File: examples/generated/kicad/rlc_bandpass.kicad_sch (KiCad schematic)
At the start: 5 parts

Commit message: Attempt to correct strange wiring.
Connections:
- net GND: no longer C1.2, L1.1, L1.2, R1.2, R2.1
- new net: C1.2, L1.1, L1.2, R1.2, R2.1
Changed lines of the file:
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@@
     (stroke (width 0) (type solid) (color 0 0 0 0))
   )
-  (wire (pts (xy 106.35 70.00) (xy 100.00 70.00))
+  (wire (pts (xy 106.35 70.00) (xy 108.50 70.00))
     (stroke (width 0) (type solid) (color 0 0 0 0))
   )
-  (wire (pts (xy 100.00 70.00) (xy 100.00 89.00))
+  (wire (pts (xy 108.50 70.00) (xy 108.50 108.00))
     (stroke (width 0) (type solid) (color 0 0 0 0))
   )
-  (wire (pts (xy 93.65 108.00) (xy 100.00 108.00))
-    (stroke (width 0) (type solid) (color 0 0 0 0))
-  )
-  (wire (pts (xy 100.00 108.00) (xy 100.00 89.00))
+  (wire (pts (xy 108.50 108.00) (xy 93.65 108.00))
     (stroke (width 0) (type solid) (color 0 0 0 0))
   )
@@
     (stroke (width 0) (type solid) (color 0 0 0 0))
   )
-  (wire (pts (xy 100.00 108.00) (xy 100.00 98.00))
+  (wire (pts (xy 100.00 108.00) (xy 100.00 127.00))
     (stroke (width 0) (type solid) (color 0 0 0 0))
   )
-  (wire (pts (xy 100.00 139.65) (xy 100.00 98.00))
+  (wire (pts (xy 100.00 139.65) (xy 100.00 127.00))
     (stroke (width 0) (type solid) (color 0 0 0 0))
   )
-  (wire (pts (xy 93.65 184.00) (xy 100.00 184.00))
+  (wire (pts (xy 93.65 184.00) (xy 91.50 184.00))
     (stroke (width 0) (type solid) (color 0 0 0 0))
   )
-  (wire (pts (xy 100.00 184.00) (xy 100.00 98.00))
+  (wire (pts (xy 91.50 184.00) (xy 91.50 127.00))
     (stroke (width 0) (type solid) (color 0 0 0 0))
   )
-  (wire (pts (xy 50.00 62.38) (xy 71.83 62.38))
+  (wire (pts (xy 91.50 127.00) (xy 100.00 127.00))
     (stroke (width 0) (type solid) (color 0 0 0 0))
   )
-  (wire (pts (xy 71.83 62.38) (xy 71.83 66.19))
+  (wire (pts (xy 50.00 62.38) (xy 50.00 70.00))
     (stroke (width 0) (type solid) (color 0 0 0 0))
   )
-  (wire (pts (xy 93.65 70.00) (xy 71.83 70.00))
+  (wire (pts (xy 50.00 70.00) (xy 93.65 70.00))
     (stroke (width 0) (type solid) (color 0 0 0 0))
   )
-  (wire (pts (xy 71.83 70.00) (xy 71.83 66.19))
-    (stroke (width 0) (type solid) (color 0 0 0 0))
-  )
-  (junction (at 100.00 98.00) (diameter 1.016) (color 0 0 0 0))
+  (junction (at 100.00 127.00) (diameter 1.016) (color 0 0 0 0))
   (sheet_instances
     (path "/" (page "1"))

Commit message: Attempt shape and wiring fixes again.
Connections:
- net GND: now also R2.1; no longer R2.2
- new net: L1.1, R1.2
- new net: C1.2, L1.2, R2.2
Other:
- moved on the sheet: C1, L1, R1, R2, V1
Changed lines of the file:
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@@
     (comment 1 "Generated by mixedsig2cad")
   )
-  (symbol (lib_id "VSOURCE") (at 50.00 70.00 180) (unit 1)
+  (symbol (lib_id "VSOURCE") (at 56.00 86.00 180) (unit 1)
     (in_bom yes) (on_board yes)
-    (property "Reference" "V1" (at 50.0 60.0 0)
+    (property "Reference" "V1" (at 56.0 76.0 0)
       (effects (font (size 1.27 1.27)))
     )
-    (property "Value" "AC 1" (at 50.0 80.0 0)
+    (property "Value" "AC 1" (at 56.0 96.0 0)
       (effects (font (size 1.27 1.27)))
     )
@@
     )
   )
-  (symbol (lib_id "R") (at 100.00 70.00 90) (unit 1)
+  (symbol (lib_id "R") (at 90.00 78.00 90) (unit 1)
     (in_bom yes) (on_board yes)
-    (property "Reference" "R1" (at 100.0 62.0 0)
+    (property "Reference" "R1" (at 90.0 70.0 0)
       (effects (font (size 1.27 1.27)))
     )
-    (property "Value" "50" (at 100.0 78.0 0)
+    (property "Value" "50" (at 90.0 86.0 0)
       (effects (font (size 1.27 1.27)))
     )
@@
     )
   )
-  (symbol (lib_id "INDUCTOR") (at 100.00 108.00 0) (unit 1)
+  (symbol (lib_id "INDUCTOR") (at 120.00 78.00 0) (unit 1)
     (in_bom yes) (on_board yes)
-    (property "Reference" "L1" (at 100.0 100.0 0)
+    (property "Reference" "L1" (at 120.0 70.0 0)
       (effects (font (size 1.27 1.27)))
     )
-    (property "Value" "10m" (at 100.0 116.0 0)
+    (property "Value" "10m" (at 120.0 86.0 0)
       (effects (font (size 1.27 1.27)))
     )
@@
     )
   )
-  (symbol (lib_id "CAP") (at 100.00 146.00 180) (unit 1)
+  (symbol (lib_id "CAP") (at 120.00 112.00 180) (unit 1)
     (in_bom yes) (on_board yes)
-    (property "Reference" "C1" (at 100.0 138.0 0)
+    (property "Reference" "C1" (at 120.0 104.0 0)
       (effects (font (size 1.27 1.27)))
     )
-    (property "Value" "100n" (at 100.0 154.0 0)
+    (property "Value" "100n" (at 120.0 120.0 0)
       (effects (font (size 1.27 1.27)))
     )
@@
     )
   )
-  (symbol (lib_id "R") (at 100.00 184.00 90) (unit 1)
+  (symbol (lib_id "R") (at 142.00 130.00 180) (unit 1)
     (in_bom yes) (on_board yes)
-    (property "Reference" "R2" (at 100.0 176.0 0)
+    (property "Reference" "R2" (at 142.0 122.0 0)
       (effects (font (size 1.27 1.27)))
     )
-    (property "Value" "1k" (at 100.0 192.0 0)
+    (property "Value" "1k" (at 142.0 138.0 0)
       (effects (font (size 1.27 1.27)))
     )
@@
     )
   )
-  (symbol (lib_id "GND") (at 50.00 89.62 0) (unit 1)
+  (symbol (lib_id "GND") (at 56.00 105.62 0) (unit 1)
     (in_bom yes) (on_board yes)
-    (property "Reference" "#PWR0001" (at 50.0 85.81 0)
+    (property "Reference" "#PWR0001" (at 56.0 101.81 0)
       (effects (font (size 1.27 1.27)) hide)
     )
-    (property "Value" "GND" (at 50.0 93.43 0)
+    (property "Value" "GND" (at 56.0 109.43 0)
       (effects (font (size 1.27 1.27)))
     )
@@
     )
   )
-  (symbol (lib_id "GND") (at 100.00 164.35 0) (unit 1)
+  (symbol (lib_id "GND") (at 120.00 130.35 0) (unit 1)
     (in_bom yes) (on_board yes)
-    (property "Reference" "#PWR0002" (at 100.0 160.54 0)
+    (property "Reference" "#PWR0002" (at 120.0 126.53999999999999 0)
       (effects (font (size 1.27 1.27)) hide)
     )
-    (property "Value" "GND" (at 100.0 168.16 0)
+    (property "Value" "GND" (at 120.0 134.16 0)
       (effects (font (size 1.27 1.27)))
     )
@@
     )
   )
-  (symbol (lib_id "GND") (at 106.35 196.00 0) (unit 1)
+  (symbol (lib_id "GND") (at 142.00 148.35 0) (unit 1)
     (in_bom yes) (on_board yes)
-    (property "Reference" "#PWR0003" (at 106.35 192.19 0)
+    (property "Reference" "#PWR0003" (at 142.0 144.54 0)
       (effects (font (size 1.27 1.27)) hide)
     )
-    (property "Value" "GND" (at 106.35 199.81 0)
+    (property "Value" "GND" (at 142.0 152.16 0)
       (effects (font (size 1.27 1.27)))
     )
@@
     )
   )
-  (wire (pts (xy 50.00 77.62) (xy 50.00 89.62))
+  (wire (pts (xy 56.00 93.62) (xy 56.00 95.50))
     (stroke (width 0) (type solid) (color 0 0 0 0))
   )
-  (wire (pts (xy 100.00 152.35) (xy 100.00 164.35))
+  (wire (pts (xy 56.00 95.50) (xy 62.00 95.50))
     (stroke (width 0) (type solid) (color 0 0 0 0))
   )
-  (wire (pts (xy 106.35 184.00) (xy 106.35 196.00))
+  (wire (pts (xy 62.00 95.50) (xy 62.00 105.62))
     (stroke (width 0) (type solid) (color 0 0 0 0))
   )
-  (wire (pts (xy 106.35 70.00) (xy 108.50 70.00))
+  (wire (pts (xy 62.00 105.62) (xy 56.00 105.62))
     (stroke (width 0) (type solid) (color 0 0 0 0))
   )
-  (wire (pts (xy 108.50 70.00) (xy 108.50 108.00))
+  (wire (pts (xy 120.00 118.35) (xy 120.00 123.35))
     (stroke (width 0) (type solid) (color 0 0 0 0))
   )
-  (wire (pts (xy 108.50 108.00) (xy 93.65 108.00))
+  (wire (pts (xy 120.00 123.35) (xy 126.00 123.35))
     (stroke (width 0) (type solid) (color 0 0 0 0))
   )
-  (wire (pts (xy 106.35 108.00) (xy 100.00 108.00))
+  (wire (pts (xy 126.00 123.35) (xy 126.00 130.35))
     (stroke (width 0) (type solid) (color 0 0 0 0))
   )
-  (wire (pts (xy 100.00 108.00) (xy 100.00 127.00))
+  (wire (pts (xy 126.00 130.35) (xy 120.00 130.35))
     (stroke (width 0) (type solid) (color 0 0 0 0))
   )
-  (wire (pts (xy 100.00 139.65) (xy 100.00 127.00))
+  (wire (pts (xy 142.00 136.35) (xy 142.00 138.50))
     (stroke (width 0) (type solid) (color 0 0 0 0))
   )
-  (wire (pts (xy 93.65 184.00) (xy 91.50 184.00))
+  (wire (pts (xy 142.00 138.50) (xy 148.00 138.50))
     (stroke (width 0) (type solid) (color 0 0 0 0))
   )
-  (wire (pts (xy 91.50 184.00) (xy 91.50 127.00))
+  (wire (pts (xy 148.00 138.50) (xy 148.00 148.35))
     (stroke (width 0) (type solid) (color 0 0 0 0))
   )
-  (wire (pts (xy 91.50 127.00) (xy 100.00 127.00))
+  (wire (pts (xy 148.00 148.35) (xy 142.00 148.35))
     (stroke (width 0) (type solid) (color 0 0 0 0))
   )
-  (wire (pts (xy 50.00 62.38) (xy 50.00 70.00))
+  (wire (pts (xy 96.35 78.00) (xy 113.65 78.00))
     (stroke (width 0) (type solid) (color 0 0 0 0))
   )
-  (wire (pts (xy 50.00 70.00) (xy 93.65 70.00))
+  (wire (pts (xy 126.35 78.00) (xy 131.00 78.00))
     (stroke (width 0) (type solid) (color 0 0 0 0))
   )
-  (junction (at 100.00 127.00) (diameter 1.016) (color 0 0 0 0))
+  (wire (pts (xy 131.00 78.00) (xy 131.00 95.00))
+    (stroke (width 0) (type solid) (color 0 0 0 0))
+  )
+  (wire (pts (xy 120.00 105.65) (xy 120.00 95.00))
+    (stroke (width 0) (type solid) (color 0 0 0 0))
+  )
+  (wire (pts (xy 120.00 95.00) (xy 131.00 95.00))
+    (stroke (width 0) (type solid) (color 0 0 0 0))
+  )
+  (wire (pts (xy 142.00 123.65) (xy 142.00 95.00))
+    (stroke (width 0) (type solid) (color 0 0 0 0))
+  )
+  (wire (pts (xy 142.00 95.00) (xy 131.00 95.00))
+    (stroke (width 0) (type solid) (color 0 0 0 0))
+  )
+  (wire (pts (xy 56.00 78.38) (xy 56.00 78.00))
+    (stroke (width 0) (type solid) (color 0 0 0 0))
+  )
+  (wire (pts (xy 56.00 78.00) (xy 83.65 78.00))
+    (stroke (width 0) (type solid) (color 0 0 0 0))
+  )
+  (junction (at 131.00 95.00) (diameter 1.016) (color 0 0 0 0))
   (sheet_instances
     (path "/" (page "1"))

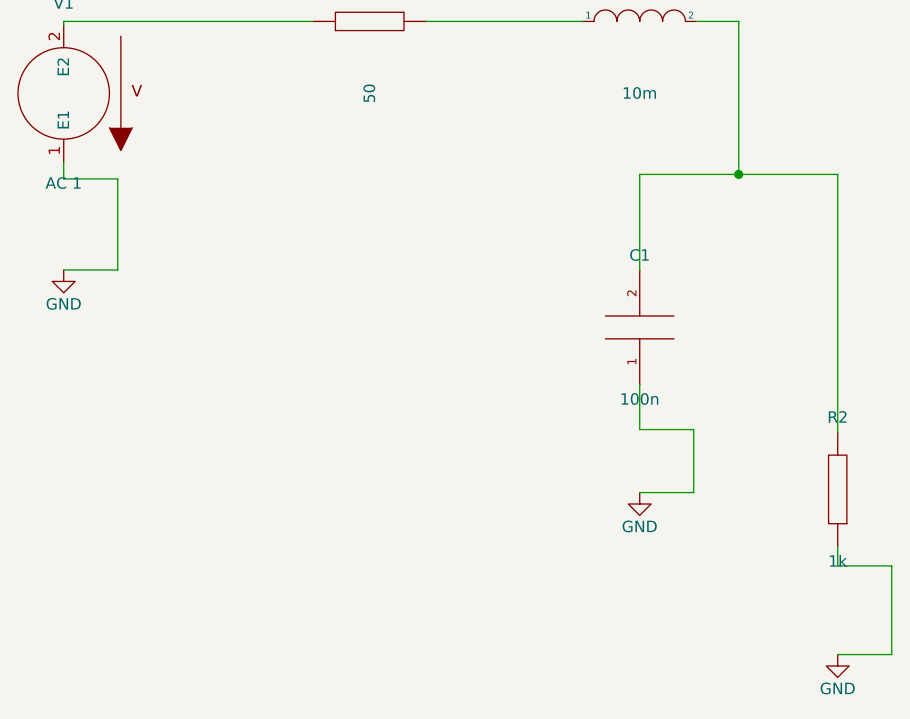
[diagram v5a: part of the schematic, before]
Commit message: Attempt to fix kinking and terminal direction issuses.
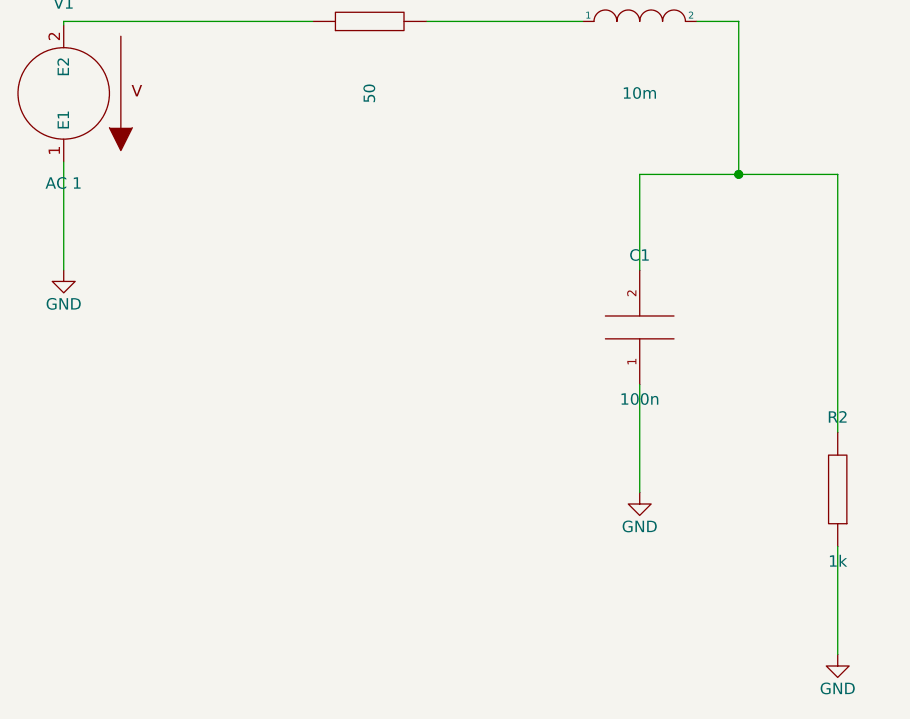
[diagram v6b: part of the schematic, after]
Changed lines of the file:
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@@
     )
   )
-  (wire (pts (xy 56.00 93.62) (xy 56.00 95.50))
+  (wire (pts (xy 56.00 93.62) (xy 56.00 105.62))
     (stroke (width 0) (type solid) (color 0 0 0 0))
   )
-  (wire (pts (xy 56.00 95.50) (xy 62.00 95.50))
+  (wire (pts (xy 120.00 118.35) (xy 120.00 130.35))
     (stroke (width 0) (type solid) (color 0 0 0 0))
   )
-  (wire (pts (xy 62.00 95.50) (xy 62.00 105.62))
+  (wire (pts (xy 142.00 136.35) (xy 142.00 148.35))
     (stroke (width 0) (type solid) (color 0 0 0 0))
   )
-  (wire (pts (xy 62.00 105.62) (xy 56.00 105.62))
-    (stroke (width 0) (type solid) (color 0 0 0 0))
-  )
-  (wire (pts (xy 120.00 118.35) (xy 120.00 123.35))
-    (stroke (width 0) (type solid) (color 0 0 0 0))
-  )
-  (wire (pts (xy 120.00 123.35) (xy 126.00 123.35))
-    (stroke (width 0) (type solid) (color 0 0 0 0))
-  )
-  (wire (pts (xy 126.00 123.35) (xy 126.00 130.35))
-    (stroke (width 0) (type solid) (color 0 0 0 0))
-  )
-  (wire (pts (xy 126.00 130.35) (xy 120.00 130.35))
-    (stroke (width 0) (type solid) (color 0 0 0 0))
-  )
-  (wire (pts (xy 142.00 136.35) (xy 142.00 138.50))
-    (stroke (width 0) (type solid) (color 0 0 0 0))
-  )
-  (wire (pts (xy 142.00 138.50) (xy 148.00 138.50))
-    (stroke (width 0) (type solid) (color 0 0 0 0))
-  )
-  (wire (pts (xy 148.00 138.50) (xy 148.00 148.35))
-    (stroke (width 0) (type solid) (color 0 0 0 0))
-  )
-  (wire (pts (xy 148.00 148.35) (xy 142.00 148.35))
-    (stroke (width 0) (type solid) (color 0 0 0 0))
-  )

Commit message: Attempt to fix more terminal issues.
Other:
- moved on the sheet: C1, R2
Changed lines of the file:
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@@
+    )
+  )
+  (symbol (lib_id "GND") (at 56.00 105.62 0) (unit 1)
+    (in_bom yes) (on_board yes)
+    (property "Reference" "#PWR0001" (at 56.0 101.81 0)
+      (effects (font (size 1.27 1.27)) hide)
+    )
+    (property "Value" "GND" (at 56.0 109.43 0)
+      (effects (font (size 1.27 1.27)))
+    )
+    (property "Footprint" "" (at 0 0 0)
+      (effects (font (size 1.27 1.27)) hide)
+    )
+    (property "Datasheet" "" (at 0 0 0)
+      (effects (font (size 1.27 1.27)) hide)
     )
   )
@@
     )
   )
-  (symbol (lib_id "CAP") (at 120.00 112.00 180) (unit 1)
+  (symbol (lib_id "CAP") (at 117.35 96.35 180) (unit 1)
     (in_bom yes) (on_board yes)
-    (property "Reference" "C1" (at 120.0 104.0 0)
+    (property "Reference" "C1" (at 117.35 88.35 0)
       (effects (font (size 1.27 1.27)))
     )
-    (property "Value" "100n" (at 120.0 120.0 0)
+    (property "Value" "100n" (at 117.35 104.35 0)
       (effects (font (size 1.27 1.27)))
     )
@@
     )
   )
-  (symbol (lib_id "R") (at 142.00 130.00 180) (unit 1)
+  (symbol (lib_id "GND") (at 117.35 114.70 0) (unit 1)
     (in_bom yes) (on_board yes)
-    (property "Reference" "R2" (at 142.0 122.0 0)
-      (effects (font (size 1.27 1.27)))
+    (property "Reference" "#PWR0002" (at 117.35 110.89 0)
+      (effects (font (size 1.27 1.27)) hide)
     )
-    (property "Value" "1k" (at 142.0 138.0 0)
+    (property "Value" "GND" (at 117.35 118.51 0)
       (effects (font (size 1.27 1.27)))
     )
@@
     )
   )
-  (symbol (lib_id "GND") (at 56.00 105.62 0) (unit 1)
+  (symbol (lib_id "R") (at 135.35 96.35 180) (unit 1)
     (in_bom yes) (on_board yes)
-    (property "Reference" "#PWR0001" (at 56.0 101.81 0)
-      (effects (font (size 1.27 1.27)) hide)
+    (property "Reference" "R2" (at 135.35 88.35 0)
+      (effects (font (size 1.27 1.27)))
     )
-    (property "Value" "GND" (at 56.0 109.43 0)
+    (property "Value" "1k" (at 135.35 104.35 0)
       (effects (font (size 1.27 1.27)))
     )
@@
     )
   )
-  (symbol (lib_id "GND") (at 120.00 130.35 0) (unit 1)
+  (symbol (lib_id "GND") (at 135.35 114.70 0) (unit 1)
     (in_bom yes) (on_board yes)
-    (property "Reference" "#PWR0002" (at 120.0 126.53999999999999 0)
+    (property "Reference" "#PWR0003" (at 135.35 110.89 0)
       (effects (font (size 1.27 1.27)) hide)
     )
-    (property "Value" "GND" (at 120.0 134.16 0)
+    (property "Value" "GND" (at 135.35 118.51 0)
       (effects (font (size 1.27 1.27)))
     )
@@
     )
   )
-  (symbol (lib_id "GND") (at 142.00 148.35 0) (unit 1)
-    (in_bom yes) (on_board yes)
-    (property "Reference" "#PWR0003" (at 142.0 144.54 0)
-      (effects (font (size 1.27 1.27)) hide)
-    )
-    (property "Value" "GND" (at 142.0 152.16 0)
-      (effects (font (size 1.27 1.27)))
-    )
-    (property "Footprint" "" (at 0 0 0)
-      (effects (font (size 1.27 1.27)) hide)
-    )
-    (property "Datasheet" "" (at 0 0 0)
-      (effects (font (size 1.27 1.27)) hide)
-    )
+  (wire (pts (xy 117.35 102.70) (xy 117.35 114.70))
+    (stroke (width 0) (type solid) (color 0 0 0 0))
+  )
+  (wire (pts (xy 135.35 102.70) (xy 135.35 114.70))
+    (stroke (width 0) (type solid) (color 0 0 0 0))
   )
   (wire (pts (xy 56.00 93.62) (xy 56.00 105.62))
-    (stroke (width 0) (type solid) (color 0 0 0 0))
-  )
-  (wire (pts (xy 120.00 118.35) (xy 120.00 130.35))
-    (stroke (width 0) (type solid) (color 0 0 0 0))
-  )
-  (wire (pts (xy 142.00 136.35) (xy 142.00 148.35))
-    (stroke (width 0) (type solid) (color 0 0 0 0))
-  )
-  (wire (pts (xy 96.35 78.00) (xy 113.65 78.00))
-    (stroke (width 0) (type solid) (color 0 0 0 0))
-  )
-  (wire (pts (xy 126.35 78.00) (xy 131.00 78.00))
-    (stroke (width 0) (type solid) (color 0 0 0 0))
-  )
-  (wire (pts (xy 131.00 78.00) (xy 131.00 95.00))
-    (stroke (width 0) (type solid) (color 0 0 0 0))
-  )
-  (wire (pts (xy 120.00 105.65) (xy 120.00 95.00))
-    (stroke (width 0) (type solid) (color 0 0 0 0))
-  )
-  (wire (pts (xy 120.00 95.00) (xy 131.00 95.00))
-    (stroke (width 0) (type solid) (color 0 0 0 0))
-  )
-  (wire (pts (xy 142.00 123.65) (xy 142.00 95.00))
-    (stroke (width 0) (type solid) (color 0 0 0 0))
-  )
-  (wire (pts (xy 142.00 95.00) (xy 131.00 95.00))
     (stroke (width 0) (type solid) (color 0 0 0 0))
   )
@@
     (stroke (width 0) (type solid) (color 0 0 0 0))
   )
-  (junction (at 131.00 95.00) (diameter 1.016) (color 0 0 0 0))
+  (wire (pts (xy 96.35 78.00) (xy 113.65 78.00))
+    (stroke (width 0) (type solid) (color 0 0 0 0))
+  )
+  (wire (pts (xy 117.35 90.00) (xy 117.35 90.35))
+    (stroke (width 0) (type solid) (color 0 0 0 0))
+  )
+  (wire (pts (xy 117.35 90.35) (xy 126.35 90.35))
+    (stroke (width 0) (type solid) (color 0 0 0 0))
+  )
+  (wire (pts (xy 126.35 90.35) (xy 126.35 78.00))
+    (stroke (width 0) (type solid) (color 0 0 0 0))
+  )
+  (wire (pts (xy 135.35 90.00) (xy 135.35 78.00))
+    (stroke (width 0) (type solid) (color 0 0 0 0))
+  )
+  (wire (pts (xy 135.35 78.00) (xy 126.35 78.00))
+    (stroke (width 0) (type solid) (color 0 0 0 0))
+  )
+  (junction (at 126.35 78.00) (diameter 1.016) (color 0 0 0 0))
   (sheet_instances
     (path "/" (page "1"))
@@
   (symbol_instances
     (path "/ff7a382b-150d-5dda-af7d-43696bfc33d8" (reference "V1") (unit 1) (value "AC 1") (footprint ""))
+    (path "/377a3052-07db-5d7e-aabd-1d809c76f718" (reference "#PWR0001") (unit 1) (value "GND") (footprint ""))
     (path "/2d26d2d6-68a6-5166-92c8-b235f4198e44" (reference "R1") (unit 1) (value "50") (footprint ""))
     (path "/d51770c5-9dd4-52f2-beba-2e847cdaa82c" (reference "L1") (unit 1) (value "10m") (footprint ""))
     (path "/cd1f9510-5b53-5cd9-9b95-17115dad0ad7" (reference "C1") (unit 1) (value "100n") (footprint ""))
+    (path "/73773ef2-52e2-515f-9193-ba4c4c232fbe" (reference "#PWR0002") (unit 1) (value "GND") (footprint ""))
     (path "/b1d9c617-2a8f-5ec8-b477-3e4c80c09fda" (reference "R2") (unit 1) (value "1k") (footprint ""))
-    (path "/377a3052-07db-5d7e-aabd-1d809c76f718" (reference "#PWR0001") (unit 1) (value "GND") (footprint ""))
-    (path "/73773ef2-52e2-515f-9193-ba4c4c232fbe" (reference "#PWR0002") (unit 1) (value "GND") (footprint ""))
     (path "/031d87f3-084d-5a64-83f1-7b1a54b82eb9" (reference "#PWR0003") (unit 1) (value "GND") (footprint ""))
   )
